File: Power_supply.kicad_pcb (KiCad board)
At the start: 2 copper layers, 140 x 40 mm, 51 parts, among them J20 HV_Transformer, J21 LV_Transformer, J22 220V, J23 Transformers, J24 Thyratrone, J25 Anodes_enable, J26 Conn_01x04, J27 Conn_01x04, J28 Conn_01x04, K2 SANYOU_SRD_Form_C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

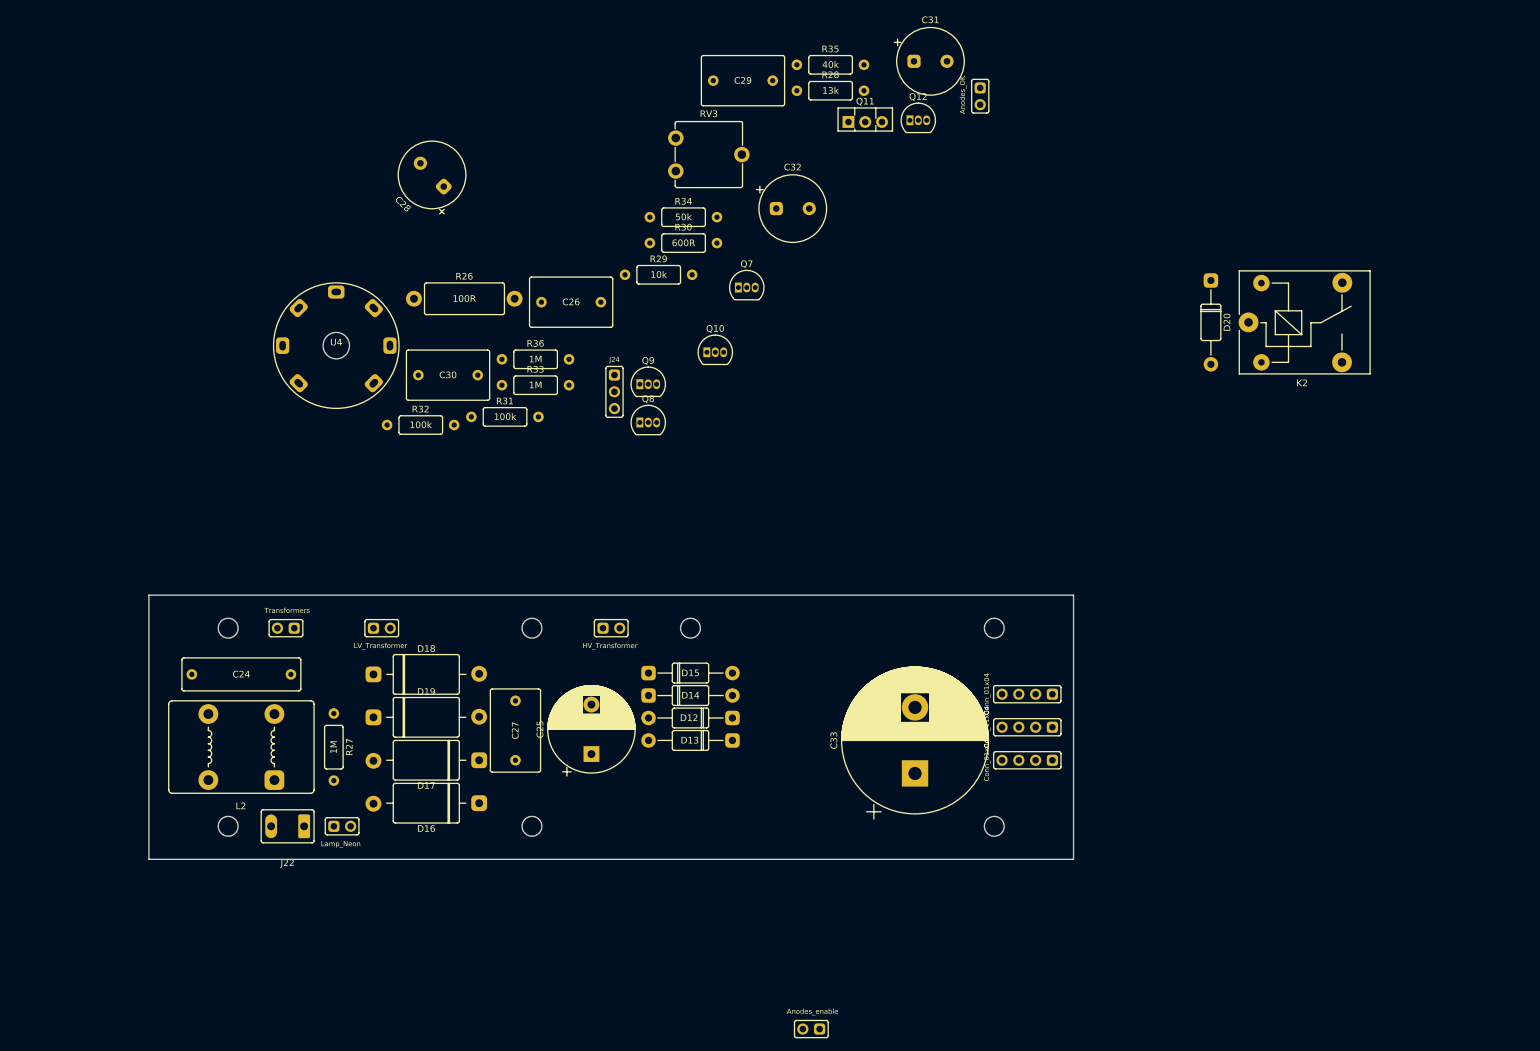
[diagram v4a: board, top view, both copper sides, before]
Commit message: New power supply
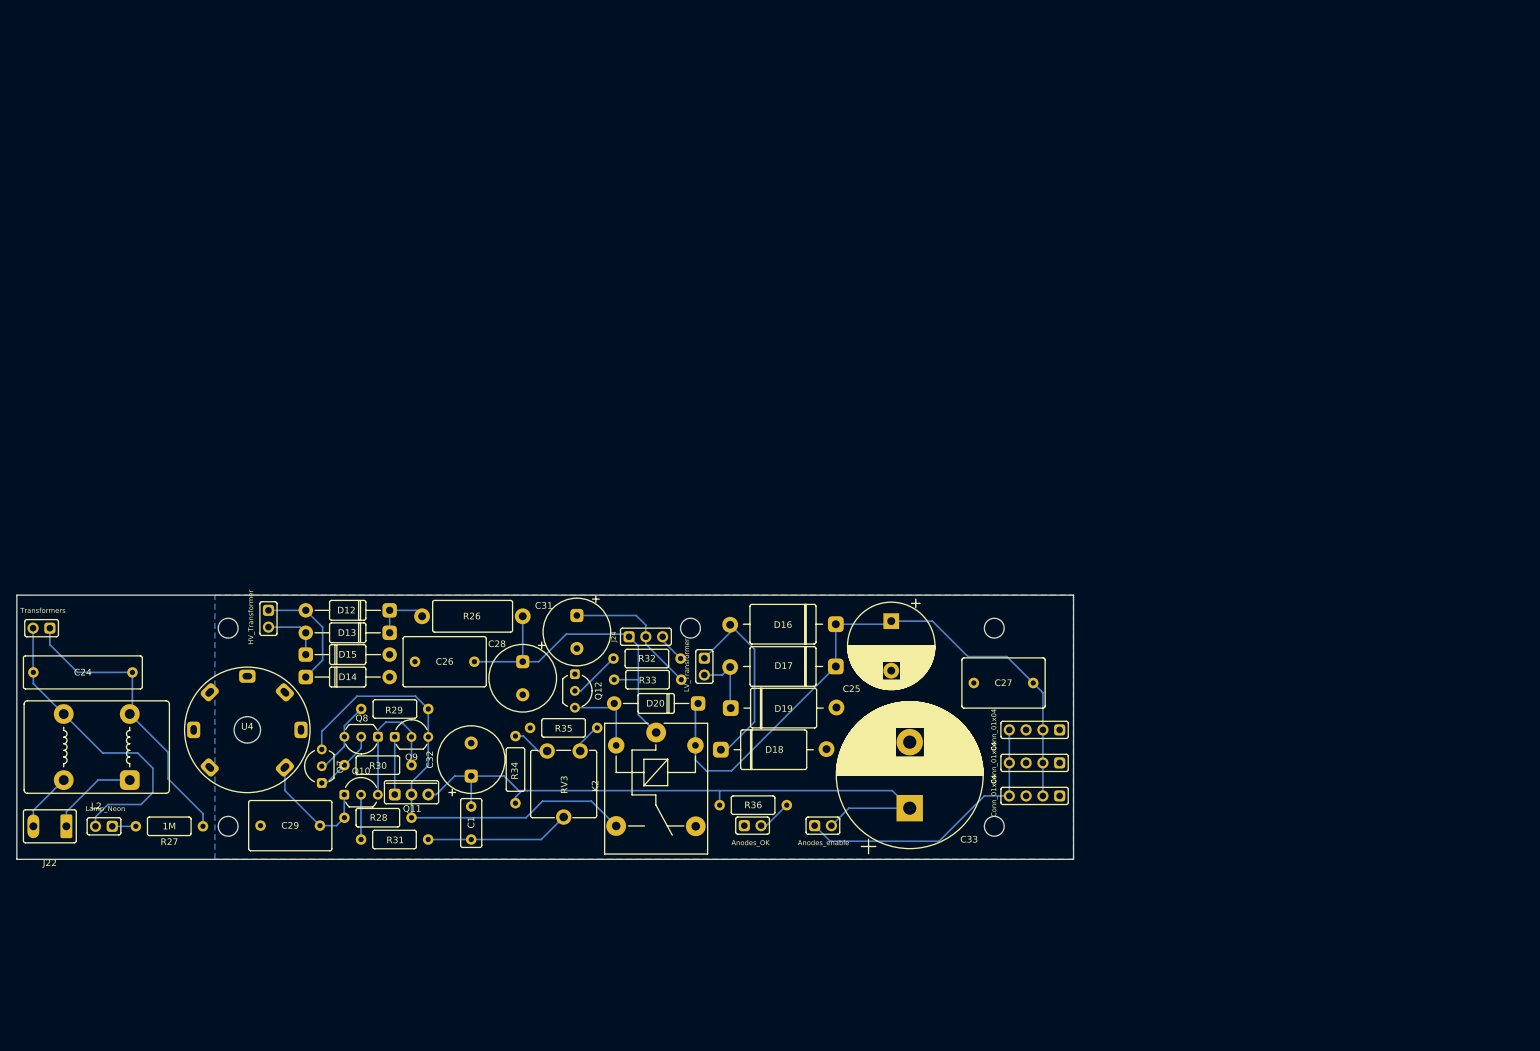
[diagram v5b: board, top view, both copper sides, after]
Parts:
- removed C30: 100n, spdf1626_lib:C_THT_K73-17_P9.00mm
- added C1: 33n, spdf1626_lib:C_THT_K73-17_P5.00mm, F.Cu at (98.8, 127.0)
- Q10, Q12, Q7, Q8, Q9: footprint Package_TO_SOT_THT:TO-92_Inline -> spdf1626_lib:TO-92_Wide
- Q11: footprint Package_TO_SOT_THT:TO-126-3_Vertical -> spdf1626_lib:TO-220_Vertical
- moved C29 132.0 mm to (71.4, 124.9)
- moved R28 124.6 mm to (89.8, 123.7), turned to 180 degrees
- moved Q11 121.4 mm to (89.8, 120.2)
- moved NE4 117.3 mm to (140.2, 124.9), turned to 90 degrees
- moved K2 109.1 mm to (126.8, 110.8), turned to -90 degrees
- moved R35 104.9 mm to (117.9, 110.1), turned to 180 degrees
- moved D20 100.7 mm to (133.2, 106.4), turned to 180 degrees
- moved Q12 100.2 mm to (114.5, 104.5), turned to -90 degrees
- moved C31 98.2 mm to (114.8, 93.1), turned to -90 degrees
- moved C32 97.6 mm to (98.8, 117.4), turned to 90 degrees
- moved Q7 96.1 mm to (76.2, 115.9), turned to 90 degrees
- moved R34 91.0 mm to (105.5, 121.5), turned to 90 degrees
- moved RV3 89.9 mm to (110.3, 113.6), turned to -90 degrees
- moved R30 86.9 mm to (89.8, 115.7), turned to 180 degrees
- moved Q10 85.0 mm to (82.1, 120.2)
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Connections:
- C28 pad 2: Net-(C28-Pad2) -> GND
- C29 pad 2: Net-(C28-Pad2) -> Net-(C29-Pad2)
- NE3 pad 2: Net-(C24-Pad2) -> Net-(C24-Pad1)
- Q10 pad 1: Net-(C28-Pad2) -> Net-(C29-Pad2)
- R27 pad 1: Net-(C24-Pad1) -> Net-(C24-Pad2)
- R28 pad 2: Net-(C28-Pad2) -> Net-(C29-Pad2)
- U4 pad 1: Net-(C28-Pad2) -> Net-(C29-Pad2)
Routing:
- net Net-(C1-Pad2): track 0.00 -> 98.2 mm
- net +6V: track 0.00 -> 95.3 mm
- net K1.1: track 0.00 -> 73.0 mm
- net HV: track 0.00 -> 52.1 mm
- net Net-(C24-Pad1): track 0.00 -> 47.1 mm
- net Net-(C24-Pad2): track 0.00 -> 44.8 mm
- net 240V: track 0.00 -> 43.3 mm
- net Net-(D16-Pad2): track 0.00 -> 29.8 mm
- net Net-(C1-Pad1): track 0.00 -> 21.9 mm
- net Net-(C31-Pad1): track 0.00 -> 21.5 mm
- net Net-(Q10-Pad3): track 0.00 -> 21.0 mm
- net Net-(C29-Pad2): track 0.00 -> 18.7 mm
- net Net-(D12-Pad2): track 0.00 -> 17.9 mm
- net Net-(J22-Pad1): track 0.00 -> 13.8 mm
- net Net-(D20-Pad2): track 0.00 -> 12.7 mm
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- added copper zone on B.Cu, net GND
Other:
- board size 140 x 40 mm -> 160 x 40 mm

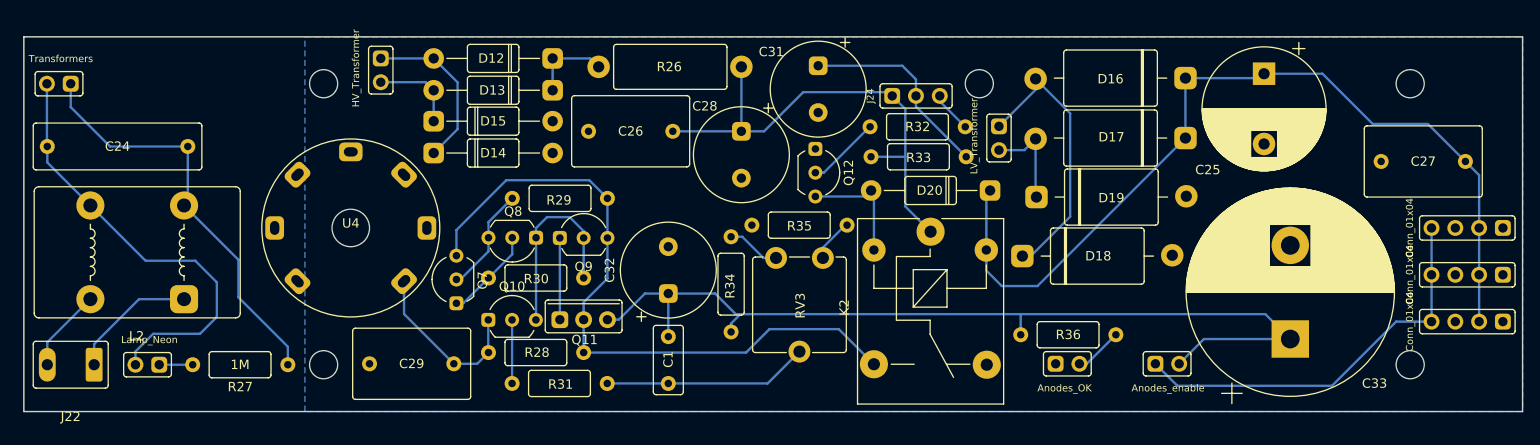
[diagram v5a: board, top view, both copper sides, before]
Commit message: Curved traces on power supply PCB
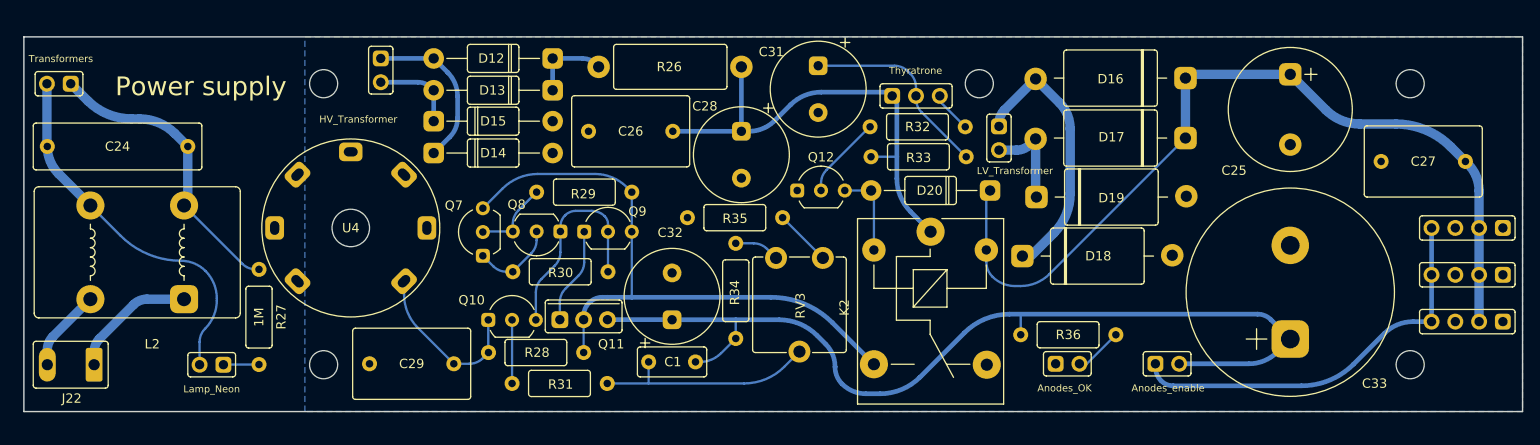
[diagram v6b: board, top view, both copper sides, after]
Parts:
- C25: footprint Capacitor_THT:CP_Radial_D13.0mm_P7.50mm -> spdf1626_lib:C_THT_D13.0mm_P7.50mm
- C33: footprint Capacitor_THT:CP_Radial_D22.0mm_P10.00mm_SnapIn -> spdf1626_lib:C_THT_D22.0mm_P10.00mm
- moved R27 10.6 mm to (55.1, 114.8), turned to -90 degrees
- moved R35 6.93 mm to (111.0, 109.3)
- moved NE3 6.85 mm to (51.3, 125.0)
- moved Q7 5.80 mm to (79.0, 110.8)
- moved C1 3.11 mm to (96.7, 124.7), turned to 0 degrees
- moved C32 2.83 mm to (99.2, 120.2)
- moved C25 2.80 mm to (165.2, 94.0)
- moved Q9 2.68 mm to (92.4, 110.8)
- moved Q8 2.68 mm to (84.7, 110.8)
- moved R29 2.68 mm to (84.7, 106.6)
- moved R30 2.68 mm to (92.4, 115.1)
- moved Q12 1.99 mm to (115.1, 106.4), turned to 0 degrees
- moved R34 0.86 mm to (106.0, 122.2)
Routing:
- net Net-(C24-Pad2): track 44.8 -> 31.9 mm
- net Net-(C24-Pad1): track 47.1 -> 40.1 mm
- net K1.1: track 73.0 -> 67.4 mm
- net Net-(C1-Pad2): track 98.2 -> 102.9 mm
- net Net-(D20-Pad2): track 12.7 -> 9.28 mm
- net Net-(Q7-Pad2): track 11.4 -> 8.38 mm
- net Net-(C1-Pad1): track 21.9 -> 23.9 mm
- net Net-(Q10-Pad3): track 21.0 -> 22.7 mm
- net Net-(R35-Pad1): track 4.49 -> 6.08 mm
- net Net-(Q11-Pad1): track 8.72 -> 10.3 mm
- net HV: track 52.1 -> 50.5 mm
- net +6V: track 95.3 -> 93.9 mm
- net Net-(Q12-Pad2): track 7.87 -> 8.90 mm
- net Net-(R34-Pad2): track 5.74 -> 4.85 mm
- net Net-(Q7-Pad1): track 9.90 -> 9.06 mm
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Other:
- board text added: "Power supply"

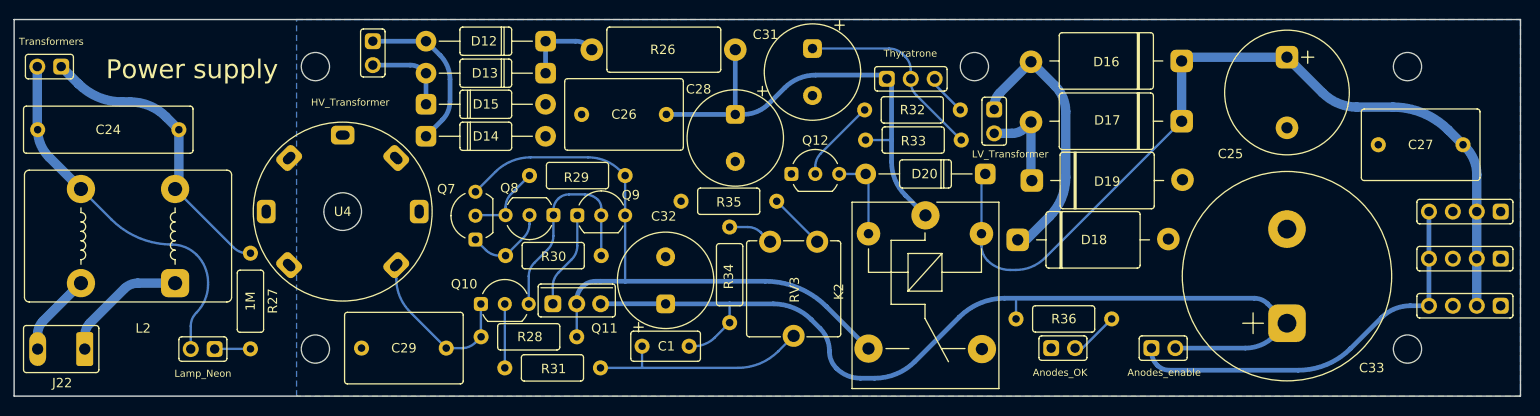
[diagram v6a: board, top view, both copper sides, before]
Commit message: New power supply schematic
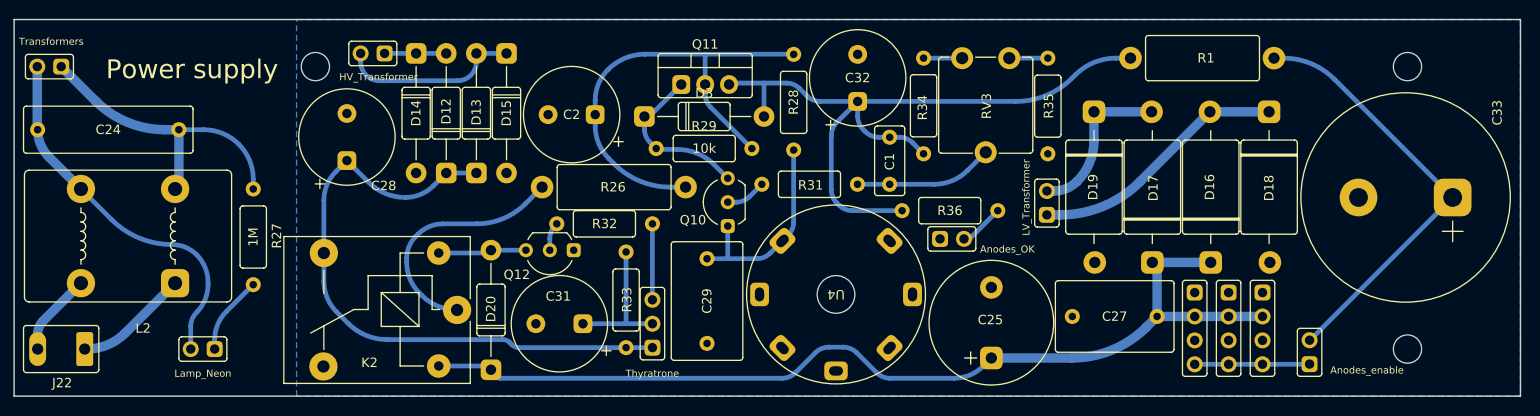
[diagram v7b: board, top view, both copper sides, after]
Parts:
- removed C26: 100n, spdf1626_lib:C_THT_K73-17_P9.00mm
- removed Q7, Q8, Q9: MPSA42, spdf1626_lib:TO-92_Wide
- removed R30: 600R, spdf1626_lib:R_THT_025W
- added C2: 10uF, spdf1626_lib:C_THT_D10.0mm_P5.00mm, F.Cu at (91.7, 100.1)
- added D3: 1N4740A, spdf1626_lib:D_DO-41, F.Cu at (97.0, 100.3)
- added R1: 100R, spdf1626_lib:R_THT_1W, F.Cu at (148.6, 94.1)
- Q11: value MJE13003 -> STP4NK60ZFP(MJE13003); footprint spdf1626_lib:TO-220_Vertical -> spdf1626_lib:TO-220-3_Vertical
- moved D20 56.5 mm to (80.6, 127.2), turned to 90 degrees
- moved U4 53.1 mm to (117.3, 119.2), turned to 180 degrees
- moved K2 50.8 mm to (77.0, 120.8), turned to 180 degrees
- moved C25 44.8 mm to (133.8, 126.0), turned to 90 degrees
- moved C28 41.5 mm to (65.3, 105.0), turned to 90 degrees
- moved C31 38.1 mm to (90.4, 122.3), turned to 180 degrees
- moved J24 37.9 mm to (97.8, 124.8), turned to 180 degrees
- moved R28 37.8 mm to (112.8, 93.7), turned to -90 degrees
- moved R33 37.5 mm to (95.0, 114.7), turned to -90 degrees
- moved C27 37.3 mm to (146.9, 121.5)
- moved R32 34.9 mm to (97.8, 111.7)
- moved J28 33.6 mm to (155.4, 119.0), turned to 0 degrees
- moved R31 33.5 mm to (119.6, 107.5)
- moved C29 32.6 mm to (103.6, 119.9), turned to 90 degrees
- moved R35 32.6 mm to (139.8, 94.1), turned to -90 degrees
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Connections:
- C33 pad 1: Net-(C1-Pad2) -> Net-(C33-Pad1)
- D12 pad 1: Net-(D12-Pad1) -> HV
- D13 pad 1: Net-(D12-Pad1) -> HV
- J25 pad 2: Net-(C1-Pad2) -> Net-(C33-Pad1)
- K2 pad 1: HV -> K1.1
- K2 pad 3: K1.1 -> HV
- Q10 pad 3: Net-(Q10-Pad3) -> Net-(D3-Pad1)
- Q11 pad 1: Net-(Q11-Pad1) -> Net-(D3-Pad1)
- Q11 pad 2: K1.1 -> Net-(C2-Pad1)
- R26 pad 1: Net-(D12-Pad1) -> K1.1
- R26 pad 2: HV -> Net-(C2-Pad1)
- R28 pad 1: K1.1 -> Net-(C2-Pad1)
- R29 pad 1: Net-(Q7-Pad2) -> Net-(D3-Pad1)
- R29 pad 2: K1.1 -> Net-(C2-Pad1)
- U4 pad 2: unconnected-(U4-Pad2) -> GND
- U4 pad 4: GND -> unconnected-(U4-Pad4)
- U4 pad 7: unconnected-(U4-Pad7) -> GND
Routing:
- net Net-(C2-Pad1): track 0.00 -> 55.2 mm
- net Net-(C33-Pad1): track 0.00 -> 46.2 mm
- net K1.1: track 67.4 -> 26.1 mm
- net 240V: track 43.2 -> 12.2 mm
- net Net-(C1-Pad2): track 102.9 -> 77.7 mm
- net Net-(Q10-Pad3): track 22.7 -> 0.00 mm
- net Net-(D3-Pad1): track 0.00 -> 17.8 mm
- net HV: track 50.5 -> 67.9 mm
- net Net-(D12-Pad2): track 17.6 -> 6.55 mm
- net +6V: track 93.9 -> 104.5 mm
- net Net-(Q11-Pad1): track 10.3 -> 0.00 mm
- net Net-(D13-Pad2): track 9.21 -> 19.4 mm
- net Net-(C1-Pad1): track 23.9 -> 14.8 mm
- net Net-(Q7-Pad1): track 9.06 -> 0.00 mm
- net Net-(D12-Pad1): track 8.59 -> 0.00 mm
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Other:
- outline, holes or cut-outs redrawn

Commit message: Wider pads
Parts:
- moved J20 4.17 mm to (68.6, 97.7), turned to 0 degrees
- moved C28 3.51 mm to (62.9, 107.5), turned to 0 degrees
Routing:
- net GND: track 0.00 -> 10.7 mm
- net Net-(D13-Pad2): track 19.4 -> 16.1 mm
- net Net-(D12-Pad2): track 6.55 -> 9.00 mm
- net HV: track 67.9 -> 69.4 mm
